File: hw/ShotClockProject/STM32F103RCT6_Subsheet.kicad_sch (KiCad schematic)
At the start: 41 parts, among them J1 USB4120-03-C_REVA, J2 Conn_ST_STDC14, J3 Conn_01x06_Pin, Q1 Q_NPN_BCE, SW1 SW_SPDT, U1 STM32F103RCT6, U2 LD39015M33R, Y1 16MHz

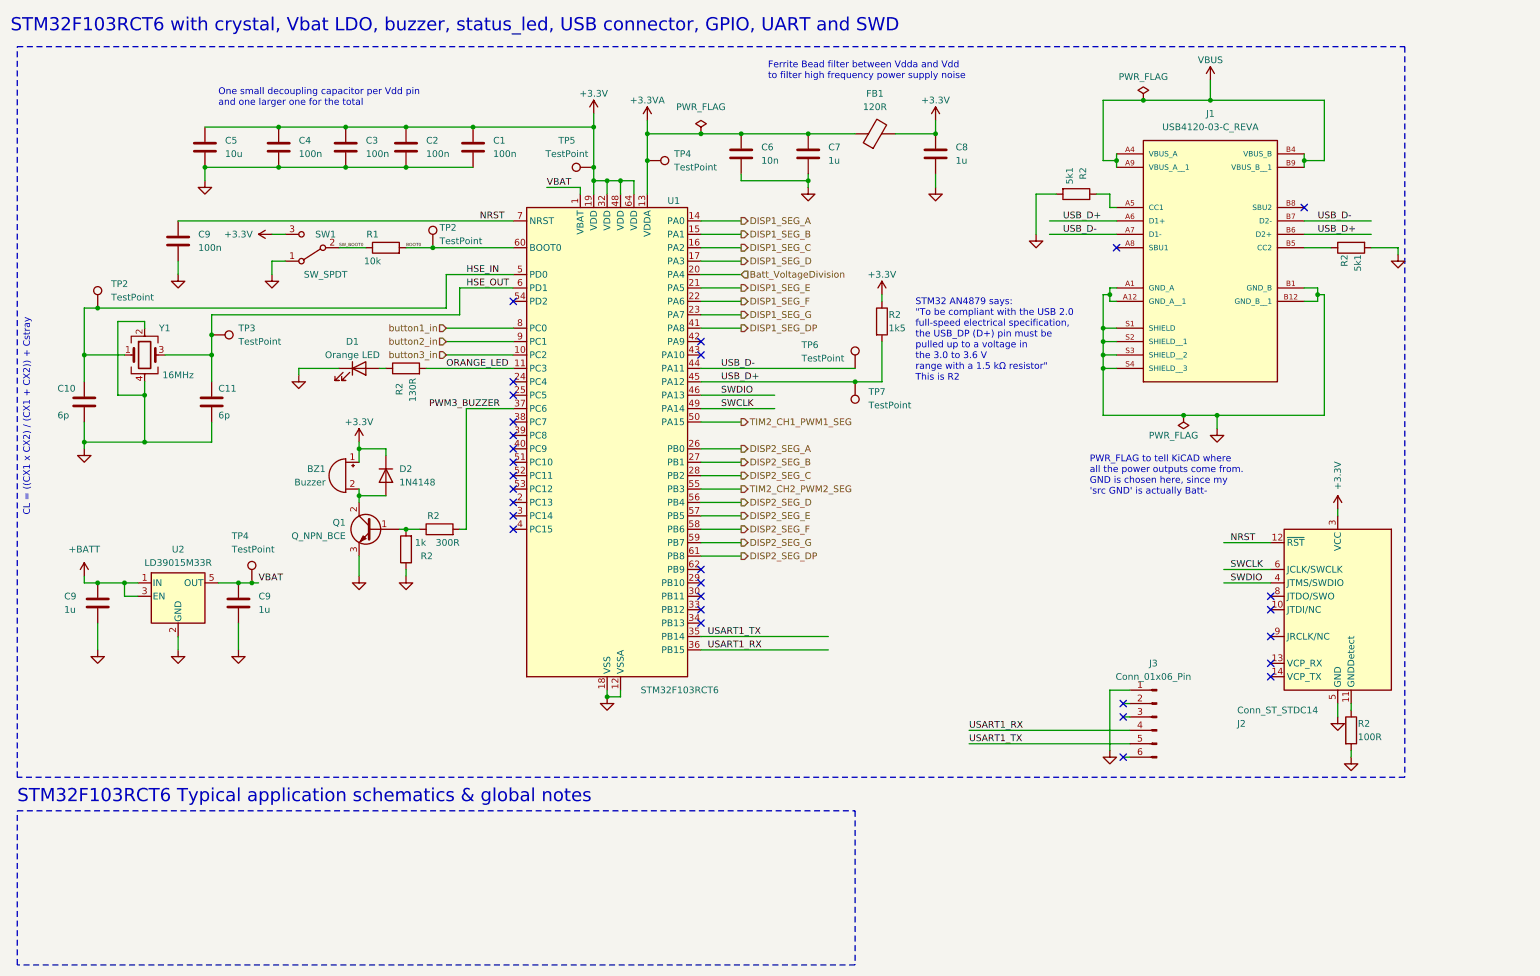
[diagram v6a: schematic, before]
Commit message: Redid layout with new board dimensions
Changed tactile switches to larger push switches (also momentary)
Changed USART1 to UART4 & added UART5 to STDC14 connector
Placed all components nearer to each other, and within the PCB outer edge
Added rounded corners
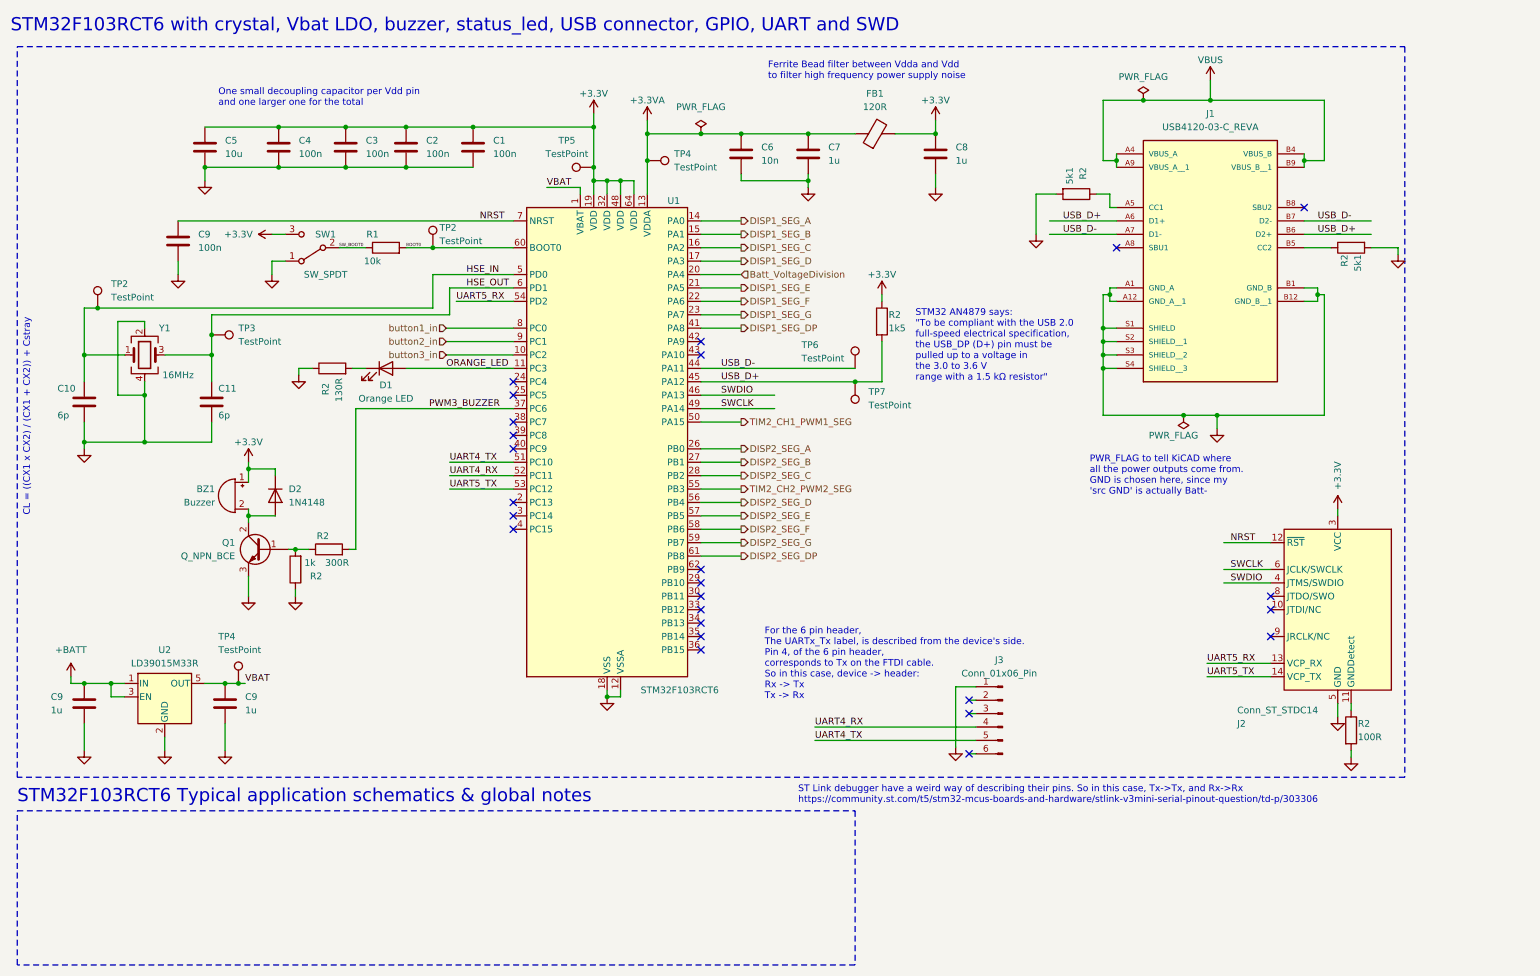
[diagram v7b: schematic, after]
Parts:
- TP2, TP3, TP4, TP5, TP6, TP7: footprint TestPoint:TestPoint_Pad_D2.5mm -> TestPoint:TestPoint_Pad_D1.0mm
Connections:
- net GND: now also R2.1; no longer D1.1 (K)
- net ORANGE_LED: now also D1.2 (A); no longer R2.2
- net UART4_TX: now reaches U1.51 (PC10)
- net UART4_TX: now also J3.5 (Pin_5)
- net UART4_RX: now reaches U1.52 (PC11)
- net UART4_RX: now also J3.4 (Pin_4)
- net UART5_TX: now reaches U1.53 (PC12)
- net UART5_TX: now also J2.14 (VCP_TX)
- net UART5_RX: now reaches U1.54 (PD2)
- net UART5_RX: now also J2.13 (VCP_RX)
- net USART1_RX: no longer names the net of U1.36 (PB15)
- net USART1_RX: no longer J3.4 (Pin_4)
- net USART1_TX: no longer names the net of U1.35 (PB14)
- net USART1_TX: no longer J3.5 (Pin_5)
- new net: D1.1 (K), R2.2
- no-connect marks 29 -> 25
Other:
- note added: "For the 6 pin header, The UARTx_Tx label, is described from the device's side. Pin 4, of the 6 pin header, corresponds to Tx on the FTDI cable. So in this case, device -> header: Rx -> Tx Tx -> Rx"
- note added: "ST Link debugger have a weird way of describing their pins. So in this case, Tx->Tx, and Rx->Rx https://community.st.com/t5/stm32-mcus-boards-and-hardware/stlink-v3mini-serial-pinout-question/td-p/303306"
- note added: "STM32 AN4879 says: "To be compliant with the USB 2.0 full-speed electrical specification, the USB_DP (D+) pin must be pulled up to a voltage in the 3.0 to 3.6 V range with a 1.5 kΩ resistor""
- note removed: "STM32 AN4879 says: "To be compliant with the USB 2.0 full-speed electrical specification, the USB_DP (D+) pin must be pulled up to a voltage in the 3.0 to 3.6 V range with a 1.5 kΩ resistor" This is R2"
- moved on the sheet: BZ1, C9, D1, D2, J3, Q1, R2, TP4, U2

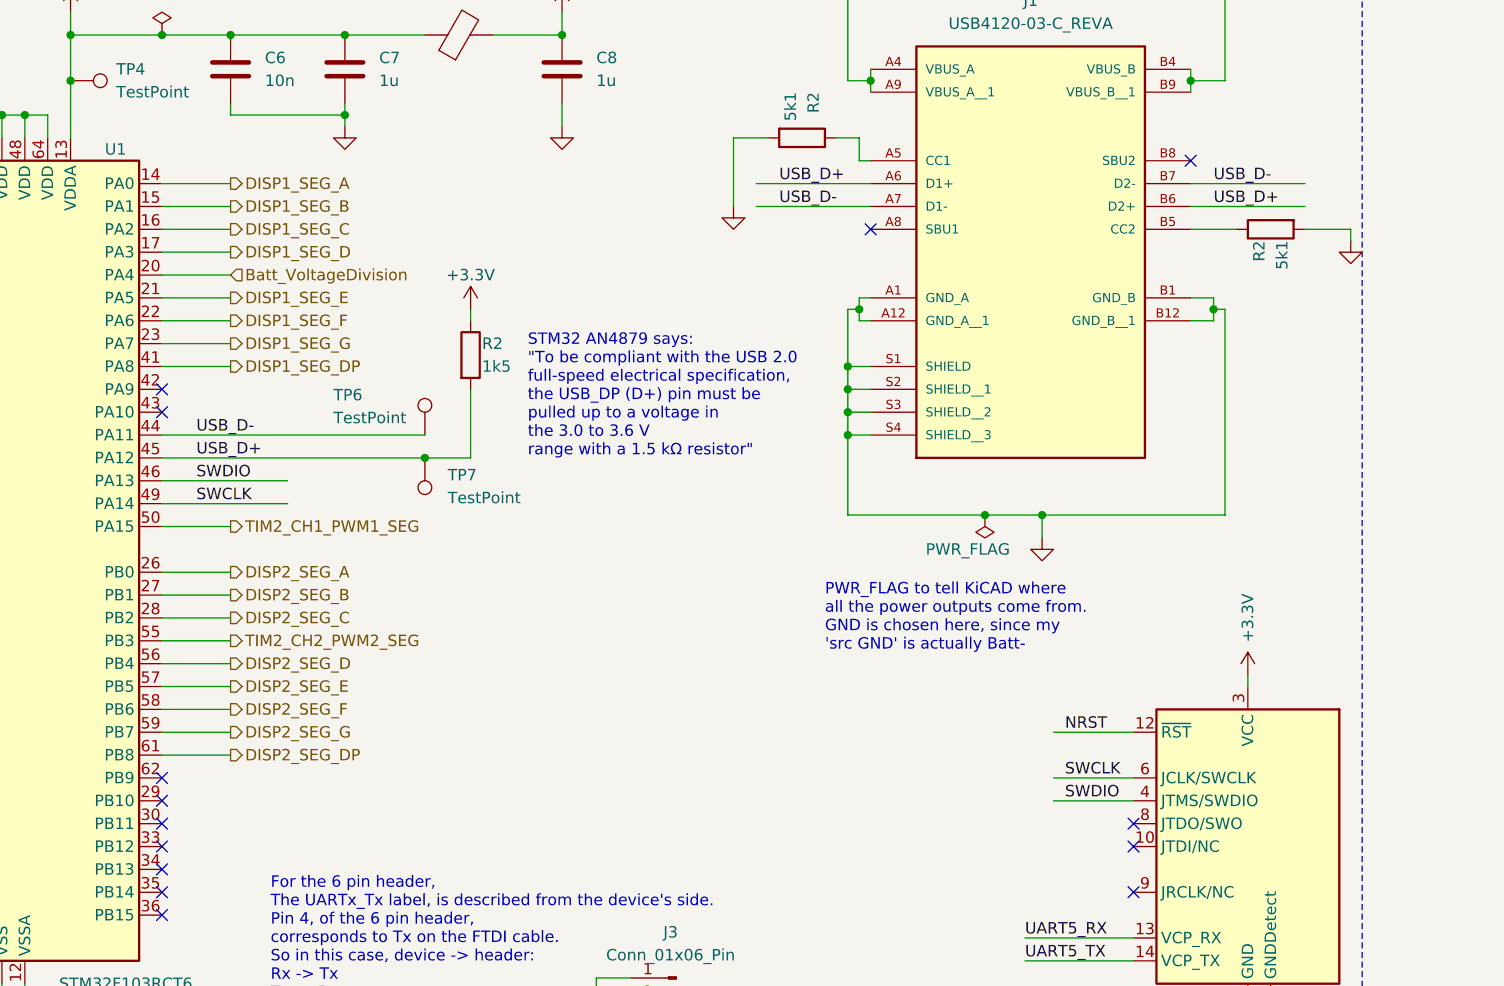
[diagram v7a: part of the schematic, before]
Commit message: Added USB ESD protection
Removed testpoints for USB+ and USB-
Removed routes to display connectors, for another try
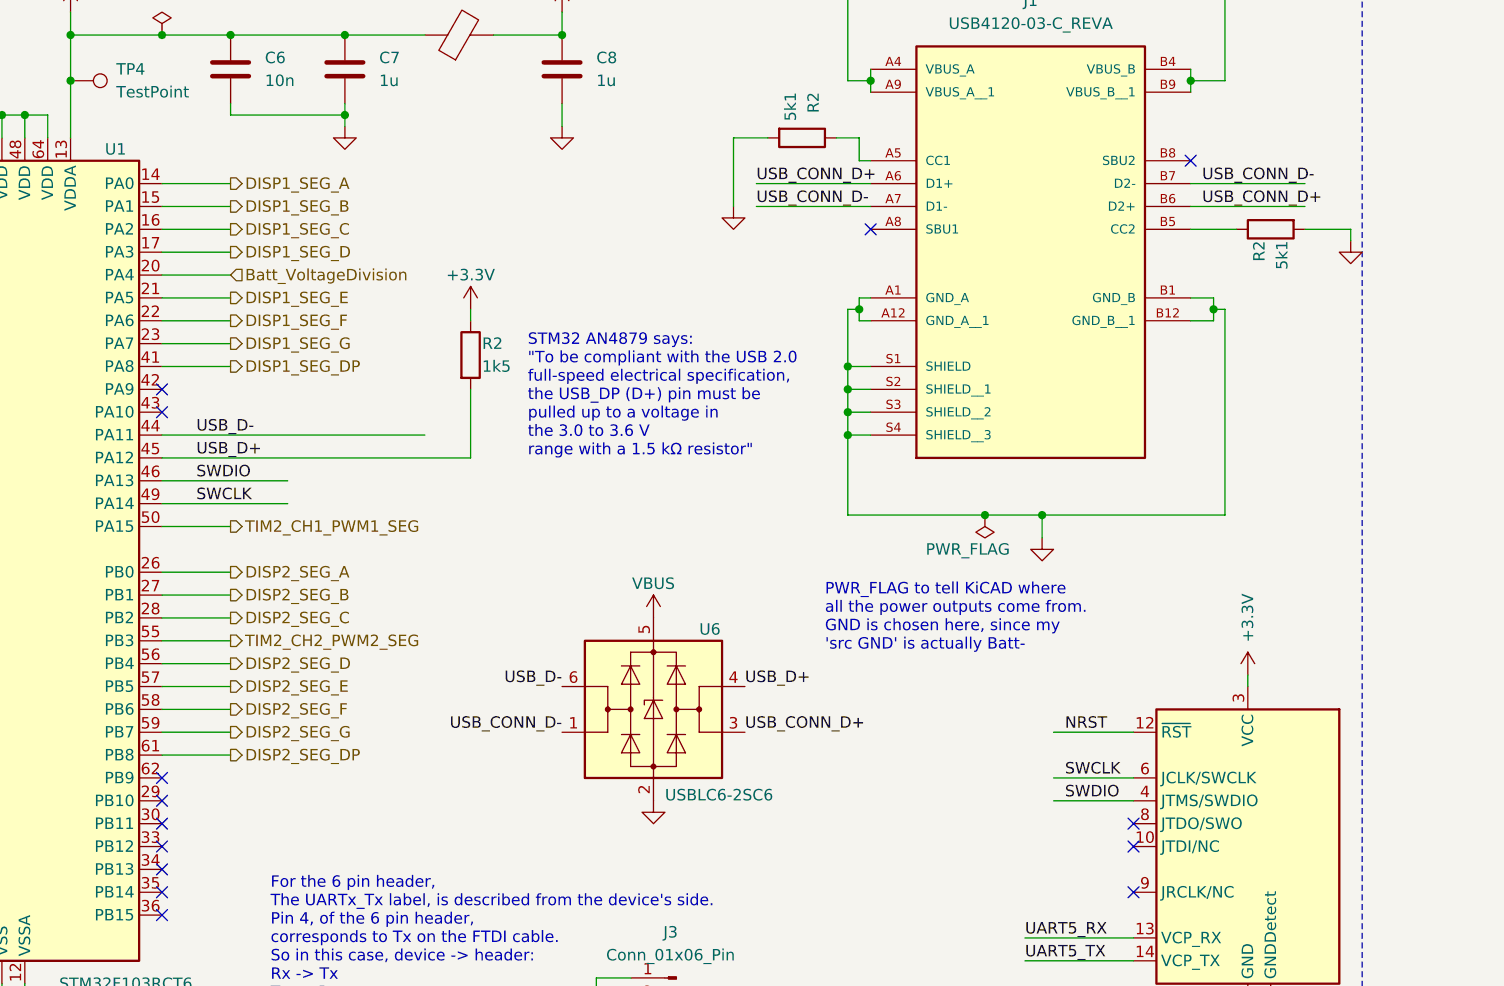
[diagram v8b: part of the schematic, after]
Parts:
- removed TP6, TP7: TestPoint, TestPoint:TestPoint_Pad_D1.0mm, symbol Connector:TestPoint
- added U6: USBLC6-2SC6, Package_TO_SOT_SMD:SOT-23-6, symbol Power_Protection:USBLC6-2SC6
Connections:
- net GND: now also U6.2 (GND)
- net USB_D+: now also U6.4 (I/O2); no longer J1.A6 (D1+), J1.B6 (D2+)
- net USB_D-: now also U6.6 (I/O1); no longer J1.A7 (D1-), J1.B7 (D2-)
- net VBUS: now also U6.5 (VBUS)
- new net USB_CONN_D+: J1.A6 (D1+), J1.B6 (D2+), U6.3 (I/O2)
- new net USB_CONN_D-: J1.A7 (D1-), J1.B7 (D2-), U6.1 (I/O1)
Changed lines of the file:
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@@
   (junction (at 127 144.78) (diameter 0) (color 0 0 0 0)
   )
-  (junction (at 173.99 85.09) (diameter 0) (color 0 0 0 0)
-  )
   (junction (at 236.22 91.44) (diameter 0) (color 0 0 0 0)
   )
@@
     (stroke (width 0) (type default))
   )
-  (wire (pts (xy 144.78 85.09) (xy 173.99 85.09))
-    (stroke (width 0) (type default))
-  )
   (wire (pts (xy 134.62 35.56) (xy 134.62 38.1))
     (stroke (width 0) (type default))
@@
     (stroke (width 0) (type default))
   )
-  (wire (pts (xy 173.99 85.09) (xy 179.07 85.09))
+  (wire (pts (xy 144.78 85.09) (xy 179.07 85.09))
     (stroke (width 0) (type default))
   )
@@
     (effects (font (size 2.5 2.5) (color 255 0 0 1)) (justify left bottom))
   )
-  (label "USB_D+" (at 213.36 54.61 0) (fields_autoplaced)
+  (label "USB_CONN_D+" (at 210.82 54.61 0) (fields_autoplaced)
     (effects (font (size 1.27 1.27)) (justify left bottom))
   )
@@
     (effects (font (size 1.27 1.27)) (justify left bottom))
   )
-  (label "USB_D-" (at 261.62 54.61 0) (fields_autoplaced)
+  (label "USB_CONN_D-" (at 260.35 54.61 0) (fields_autoplaced)
     (effects (font (size 1.27 1.27)) (justify left bottom))
   )
@@
     (effects (font (size 1.27 1.27)) (justify left bottom))
   )
+  (label "USB_CONN_D+" (at 209.55 115.57 0) (fields_autoplaced)
+    (effects (font (size 1.27 1.27)) (justify left bottom))
+  )
   (label "UART4_RX" (at 166.37 150.495 0) (fields_autoplaced)
     (effects (font (size 1.27 1.27)) (justify left bottom))
@@
     (effects (font (size 1.27 1.27)) (justify left bottom))
   )
-  (label "USB_D-" (at 213.36 57.15 0) (fields_autoplaced)
+  (label "USB_CONN_D-" (at 210.82 57.15 0) (fields_autoplaced)
     (effects (font (size 1.27 1.27)) (justify left bottom))
   )
+  (label "USB_D-" (at 189.23 110.49 180) (fields_autoplaced)
+    (effects (font (size 1.27 1.27)) (justify right bottom))
+  )
   (label "NRST" (at 102.87 54.61 0) (fields_autoplaced)
     (effects (font (size 1.27 1.27)) (justify left bottom))
@@
     (effects (font (size 1.27 1.27)) (justify left bottom))
   )
+  (label "USB_CONN_D-" (at 189.23 115.57 180) (fields_autoplaced)
+    (effects (font (size 1.27 1.27)) (justify right bottom))
+  )
   (label "VBAT" (at 115.57 48.26 0) (fields_autoplaced)
     (effects (font (size 1.27 1.27)) (justify left bottom))
@@
     (effects (font (size 1.27 1.27)) (justify left bottom))
   )
-  (label "USB_D+" (at 261.62 57.15 0) (fields_autoplaced)
+  (label "USB_D+" (at 209.55 110.49 0) (fields_autoplaced)
+    (effects (font (size 1.27 1.27)) (justify left bottom))
+  )
+  (label "USB_CONN_D+" (at 260.35 57.15 0) (fields_autoplaced)
     (effects (font (size 1.27 1.27)) (justify left bottom))
   )
@@
     )
   )
-  (symbol (lib_id "Connector:TestPoint") (at 173.99 82.55 0) (unit 1)
-    (in_bom yes) (on_board yes) (dnp no)
-    (property "Reference" "TP6" (at 163.83 78.105 0)
-      (effects (font (size 1.27 1.27)) (justify left))
-    )
-    (property "Value" "TestPoint" (at 163.83 80.645 0)
-      (effects (font (size 1.27 1.27)) (justify left))
-    )
-    (property "Footprint" "TestPoint:TestPoint_Pad_D1.0mm" (at 179.07 82.55 0)
-      (effects (font (size 1.27 1.27)) hide)
-    )
-    (property "Datasheet" "~" (at 179.07 82.55 0)
-      (effects (font (size 1.27 1.27)) hide)
-    )
-    (pin "1")
-    (instances
-      (project "ShotClockProject"
-        (path "/5fd859aa-754d-49c2-9762-3f7ebe3bb64c"
-          (reference "TP6") (unit 1)
-        )
-        (path "/5fd859aa-754d-49c2-9762-3f7ebe3bb64c/d53b1cd8-24cb-4dc0-9a02-0cd96c1f4291"
-          (reference "TP9") (unit 1)
-        )
-      )
-    )
-  )
   (symbol (lib_id "Device:C") (at 50.8 40.64 0) (unit 1)
     (in_bom yes) (on_board yes) (dnp no) (fields_autoplaced)
@@
     )
   )
+  (symbol (lib_id "power:GND") (at 199.39 123.19 0) (unit 1)
+    (in_bom yes) (on_board yes) (dnp no) (fields_autoplaced)
+    (property "Reference" "#PWR012" (at 199.39 129.54 0)
+      (effects (font (size 1.27 1.27)) hide)
+    )
+    (property "Value" "GND" (at 199.39 128.27 0)
+      (effects (font (size 1.27 1.27)) hide)
+    )
+    (property "Footprint" "" (at 199.39 123.19 0)
+      (effects (font (size 1.27 1.27)) hide)
+    )
+    (property "Datasheet" "" (at 199.39 123.19 0)
+      (effects (font (size 1.27 1.27)) hide)
+    )
+    (pin "1")
+    (instances
+      (project "ShotClockProject"
+        (path "/5fd859aa-754d-49c2-9762-3f7ebe3bb64c"
+          (reference "#PWR012") (unit 1)
+        )
+        (path "/5fd859aa-754d-49c2-9762-3f7ebe3bb64c/d53b1cd8-24cb-4dc0-9a02-0cd96c1f4291"
+          (reference "#PWR087") (unit 1)
+        )
+      )
+    )
+  )
   (symbol (lib_id "Device:C") (at 27.94 88.9 0) (unit 1)
     (in_bom yes) (on_board yes) (dnp no)
@@
     )
   )
+  (symbol (lib_id "power:VBUS") (at 199.39 102.87 0) (unit 1)
+    (in_bom yes) (on_board yes) (dnp no)
+    (property "Reference" "#PWR013" (at 199.39 106.68 0)
+      (effects (font (size 1.27 1.27)) hide)
+    )
+    (property "Value" "VBUS" (at 199.39 99.06 0)
+      (effects (font (size 1.27 1.27)))
+    )
+    (property "Footprint" "" (at 199.39 102.87 0)
+      (effects (font (size 1.27 1.27)) hide)
+    )
+    (property "Datasheet" "" (at 199.39 102.87 0)
+      (effects (font (size 1.27 1.27)) hide)
+    )
+    (pin "1")
+    (instances
+      (project "ShotClockProject"
+        (path "/5fd859aa-754d-49c2-9762-3f7ebe3bb64c"
+          (reference "#PWR013") (unit 1)
+        )
+        (path "/5fd859aa-754d-49c2-9762-3f7ebe3bb64c/d53b1cd8-24cb-4dc0-9a02-0cd96c1f4291"
+          (reference "#PWR086") (unit 1)
+        )
+      )
+    )
+  )
   (symbol (lib_id "power:GND") (at 193.04 154.305 0) (unit 1)
     (in_bom yes) (on_board yes) (dnp no) (fields_autoplaced)
@@
     )
   )
+  (symbol (lib_id "Power_Protection:USBLC6-2SC6") (at 199.39 113.03 0) (unit 1)
+    (in_bom yes) (on_board yes) (dnp no)
+    (property "Reference" "U6" (at 204.47 104.14 0)
+      (effects (font (size 1.27 1.27)) (justify left))
+    )
+    (property "Value" "USBLC6-2SC6" (at 200.66 122.555 0)
+      (effects (font (size 1.27 1.27)) (justify left))
+    )
+    (property "Footprint" "Package_TO_SOT_SMD:SOT-23-6" (at 199.39 125.73 0)
+      (effects (font (size 1.27 1.27)) hide)
+    )
+    (property "Datasheet" "https://www.st.com/resource/en/datasheet/usblc6-2.pdf" (at 204.47 104.14 0)
+      (effects (font (size 1.27 1.27)) hide)
+    )
+    (pin "1")
+    (pin "2")
+    (pin "3")
+    (pin "4")
+    (pin "5")
+    (pin "6")
+    (instances
+      (project "ShotClockProject"
+        (path "/5fd859aa-754d-49c2-9762-3f7ebe3bb64c/d53b1cd8-24cb-4dc0-9a02-0cd96c1f4291"
+          (reference "U6") (unit 1)
+        )
+      )
+    )
+  )
   (symbol (lib_id "Diode:1N4148") (at 64.135 106.68 270) (unit 1)
     (in_bom yes) (on_board yes) (dnp no) (fields_autoplaced)
@@
         )
       )
-    )
-  )
-  (symbol (lib_id "Connector:TestPoint") (at 173.99 85.09 180) (unit 1)
-    (in_bom yes) (on_board yes) (dnp no)
-    (property "Reference" "TP7" (at 176.53 86.995 0)
-      (effects (font (size 1.27 1.27)) (justify right))
-    )
-    (property "Value" "TestPoint" (at 176.53 89.535 0)
-      (effects (font (size 1.27 1.27)) (justify right))
-    )
-    (property "Footprint" "TestPoint:TestPoint_Pad_D1.0mm" (at 168.91 85.09 0)
-      (effects (font (size 1.27 1.27)) hide)
-    )
-    (property "Datasheet" "~" (at 168.91 85.09 0)
-      (effects (font (size 1.27 1.27)) hide)
-    )
-    (pin "1")
-    (instances
-      (project "ShotClockProject"
-        (path "/5fd859aa-754d-49c2-9762-3f7ebe3bb64c"
-          (reference "TP7") (unit 1)
-        )
-        (path "/5fd859aa-754d-49c2-9762-3f7ebe3bb64c/d53b1cd8-24cb-4dc0-9a02-0cd96c1f4291"
-          (reference "TP10") (unit 1)
-        )
-      )
